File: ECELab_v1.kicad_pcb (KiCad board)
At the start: 2 copper layers, 121 parts, among them J201 USB_C_Receptacle_USB2.0, J202 Conn_01x02_Male, J301 Conn_01x04_Male, J302 Conn_01x03_Male, J501 Conn_01x12_Male, SW301 SW_SPDT, U201 AZ1117IH-3.3TRG1, U301 SN74LVC257AD, U302 FT232HL, U303 93LC56BT-I/OT, U401 MCP23S17_SS, U402 MCP23S17_SS, U403 MCP23S17_SS, U404 MCP23S17_SS, U405 MCP23S17_SS, U406 MCP23S17_SS, U407 MCP23S17_SS, U408 MCP23S17_SS, U501 ICE40-HX8K_Breakout_Board, Y301 12MHz

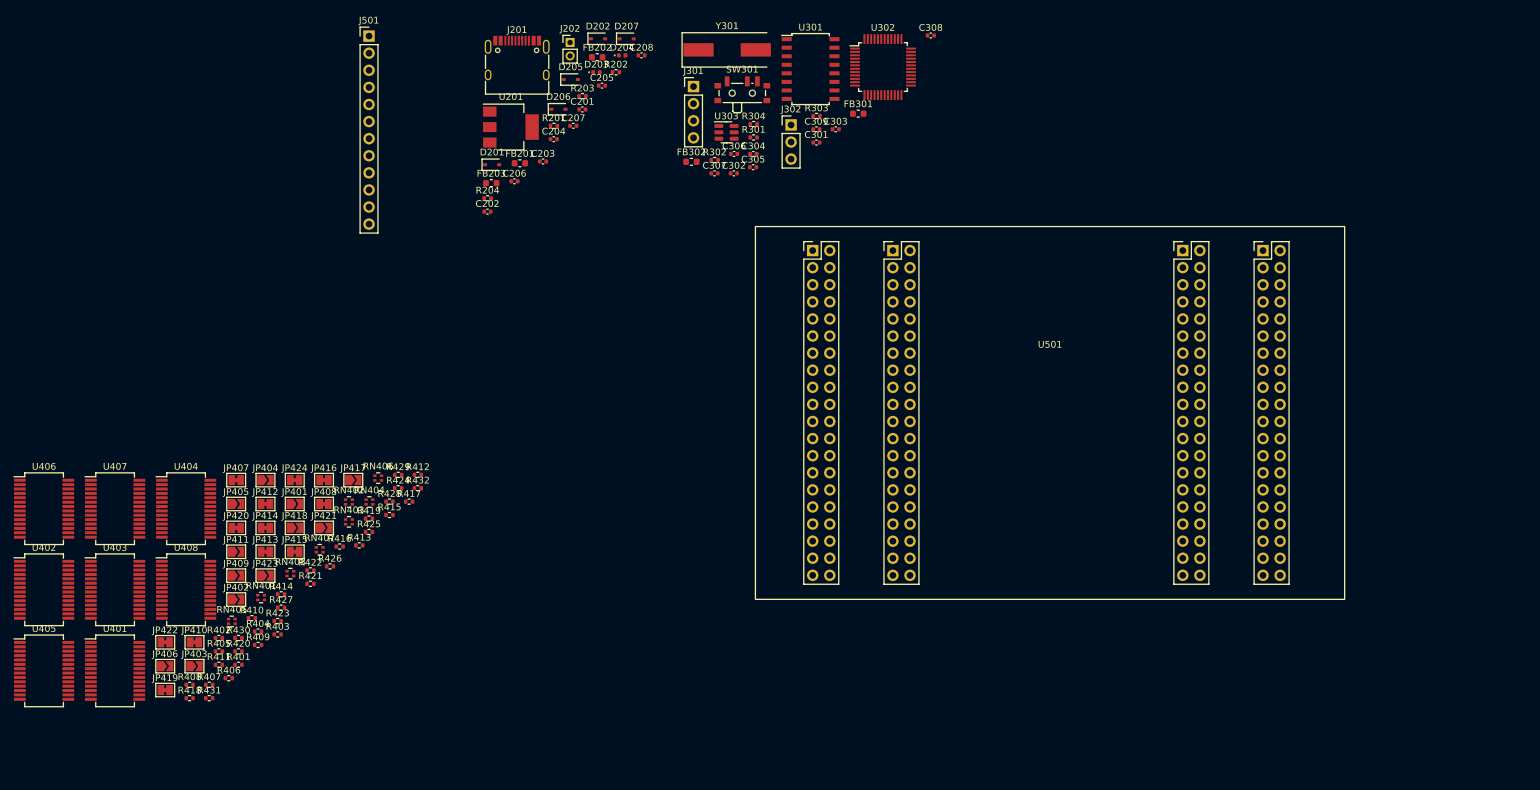
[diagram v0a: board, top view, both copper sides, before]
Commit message: Complete SPI Design
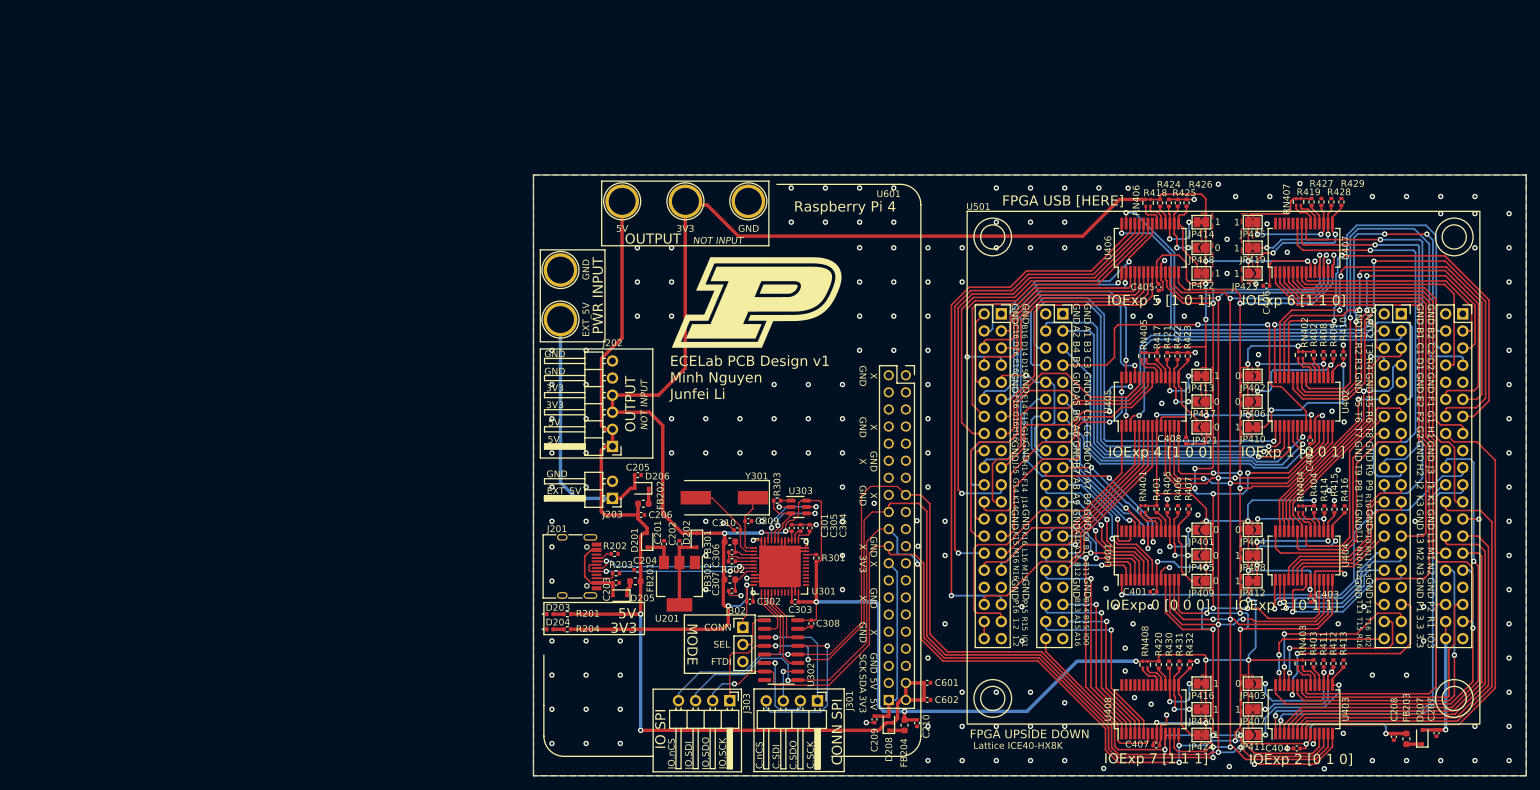
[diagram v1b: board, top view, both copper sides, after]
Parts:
- removed J501: Conn_01x12_Male, Connector_PinHeader_2.54mm:PinHeader_1x12_P2.54mm_Vertical
- removed the R303 at (146.0, 54.1)
- removed SW301: SW_SPDT, Button_Switch_SMD:SW_SPDT_PCM12
- removed the U301 at (145.1, 47.1)
- added C209: 0.1u, Capacitor_SMD:C_0402_1005Metric, F.Cu at (154.6, 143.7)
- added C210: 0.1u, Capacitor_SMD:C_0402_1005Metric, F.Cu at (160.9, 144.3)
- added C308: 0.1u, Capacitor_SMD:C_0402_1005Metric, F.Cu at (145.2, 129.5)
- added C401: 0.1u, Capacitor_SMD:C_0402_1005Metric, F.Cu at (196.1, 124.8)
- added C402: 0.1u, Capacitor_SMD:C_0402_1005Metric, F.Cu at (219.3, 102.3)
- added C403: 0.1u, Capacitor_SMD:C_0402_1005Metric, F.Cu at (219.4, 125.8)
- added C404: 0.1u, Capacitor_SMD:C_0402_1005Metric, F.Cu at (217.4, 148.1)
- added C405: 0.1u, Capacitor_SMD:C_0402_1005Metric, F.Cu at (196.8, 79.5)
- added C406: 0.1u, Capacitor_SMD:C_0402_1005Metric, F.Cu at (212.9, 79.3)
- added C407: 0.1u, Capacitor_SMD:C_0402_1005Metric, F.Cu at (196.5, 147.6)
- added C408: 0.1u, Capacitor_SMD:C_0402_1005Metric, F.Cu at (200.9, 102.3)
- added C601: 0.1u, Capacitor_SMD:C_0402_1005Metric, F.Cu at (162.5, 138.3)
- added C602: 0.1u, Capacitor_SMD:C_0402_1005Metric, F.Cu at (162.5, 140.8)
- added D208: PMEG40, Diode_SMD:D_SOD-323, F.Cu at (156.8, 144.3)
- added FB204: 120R, Inductor_SMD:L_0603_1608Metric, F.Cu at (159.1, 144.6)
- added G***: LOGO, ECELab_Footprints:purduelogo, F.Cu at (137.2, 81.8)
- added G***: LOGO, ECELab_Footprints:purduelogo, B.Cu at (137.9, 81.8)
- added J202: Conn_01x06_Male, Connector_PinHeader_2.54mm:PinHeader_1x06_P2.54mm_Horizontal, F.Cu at (115.7, 103.2)
- added J303: Conn_01x04_Male, Connector_PinHeader_2.54mm:PinHeader_1x04_P2.54mm_Horizontal, F.Cu at (133.1, 141.0)
- added TP201: TestPoint, TestPoint:TestPoint_Plated_Hole_D4.0mm, F.Cu at (117.1, 66.8)
- added TP202: TestPoint, TestPoint:TestPoint_Plated_Hole_D4.0mm, F.Cu at (126.5, 66.8)
- added TP203: TestPoint, TestPoint:TestPoint_Plated_Hole_D4.0mm, F.Cu at (135.9, 66.8)
- added TP204: TestPoint, TestPoint:TestPoint_Plated_Hole_D4.0mm, F.Cu at (108.0, 84.3)
- added TP205: TestPoint, TestPoint:TestPoint_Plated_Hole_D4.0mm, F.Cu at (108.0, 77.0)
- added U302: SN74LVC157ADR, Package_SO:SOIC-16_3.9x9.9mm_P1.27mm, F.Cu at (140.7, 133.5)
- added U601: RASPBERRY_PI_4B_4GB, ECELab_Footprints:MODULE_RASPBERRY_PI_4B_4GB, F.Cu at (134.3, 107.5)
- J203: renamed from J202; footprint Connector_PinHeader_2.00mm:PinHeader_1x02_P2.00mm_Vertical -> Connector_PinHeader_2.54mm:PinHeader_1x02_P2.54mm_Horizontal
- J301: footprint Connector_PinHeader_2.54mm:PinHeader_1x04_P2.54mm_Vertical -> Connector_PinHeader_2.54mm:PinHeader_1x04_P2.54mm_Horizontal
- R201: value 250 -> 220
- U301: renamed from U302; value FT232HL -> FT232HQ-REEL; footprint Package_QFP:LQFP-48_7x7mm_P0.5mm -> Package_DFN_QFN:QFN-48-1EP_8x8mm_P0.5mm_EP6.2x6.2mm
- U401, U402, U403, U404, U405, U406, U407, U408: value MCP23S17_SS -> MCP23017_SS
- moved U402 189.3 mm to (218.4, 96.5), turned to 90 degrees
- moved U407 180.9 mm to (218.4, 73.7), turned to 90 degrees
- moved U403 177.6 mm to (218.4, 142.2), turned to 90 degrees
- moved R408 175.5 mm to (221.3, 89.6), turned to 90 degrees
- moved JP419 174.5 mm to (210.8, 73.7)
- moved U405 169.2 mm to (195.6, 96.5), turned to 90 degrees
- moved U406 168.9 mm to (195.6, 73.7), turned to 90 degrees
- moved R402 168.1 mm to (219.9, 89.6), turned to -90 degrees
- moved R410 166.9 mm to (224.3, 89.6), turned to 90 degrees
- moved JP406 166.3 mm to (210.8, 96.5)
- moved U404 166.3 mm to (218.4, 119.4), turned to 90 degrees
- moved R427 165.9 mm to (221.0, 66.8), turned to 90 degrees
- moved R409 165.5 mm to (222.8, 89.6), turned to 90 degrees
- moved R411 164.2 mm to (221.4, 135.4), turned to 90 degrees
- moved JP422 163.5 mm to (203.2, 77.5), turned to 180 degrees
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- renumbered C308 to C309, C309 to C310, R304 to R303
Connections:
- net IO44 renamed IO.SS2_4
- J301 pad 2: CONN.SDI -> CONN.SDO
- J301 pad 3: CONN.SDO -> CONN.SDI
- J302 pad 2: MUX.SEL -> SEL
- U301 pad 14: FTDI.SDI -> FTDI.SDO
- U301 pad 15: FTDI.SDO -> FTDI.SDI
- U401 pad 1: IO0 -> IO.HWCLK
- U401 pad 13: IO.SDI -> IO.SDO
- U401 pad 14: IO.SDO -> IO.SDI
- U401 pad 2: IO1 -> IO.PB20
- U401 pad 21: IO8 -> IO.PB13
- U401 pad 22: IO9 -> IO.PB12
- U401 pad 23: IO10 -> IO.PB11
- U401 pad 24: IO11 -> IO.PB10
- U401 pad 25: IO12 -> IO.PB9
- U401 pad 26: IO13 -> IO.PB8
- U401 pad 27: IO14 -> unconnected-(U401-Pad27)
- U401 pad 28: IO15 -> unconnected-(U401-Pad28)
- U401 pad 3: IO2 -> IO.PB19
- U401 pad 4: IO3 -> IO.PB18
- U401 pad 5: IO4 -> IO.PB17
- U401 pad 6: IO5 -> IO.PB16
- U401 pad 7: IO6 -> IO.PB15
- U401 pad 8: IO7 -> IO.PB14
- U402 pad 1: IO16 -> IO.PB7
- U402 pad 13: IO.SDI -> IO.SDO
- U402 pad 14: IO.SDO -> IO.SDI
- U402 pad 2: IO17 -> IO.PB6
- U402 pad 21: IO24 -> IO.SS0_0
- U402 pad 22: IO25 -> IO.SS0_1
- U402 pad 23: IO26 -> IO.SS0_2
- U402 pad 24: IO27 -> IO.SS0_3
- U402 pad 25: IO28 -> IO.SS0_4
- U402 pad 26: IO29 -> IO.SS0_5
- U402 pad 27: IO30 -> IO.SS0_6
- U402 pad 28: IO31 -> IO.SS0_7
- U402 pad 3: IO18 -> IO.PB5
- U402 pad 4: IO19 -> IO.PB4
- U402 pad 5: IO20 -> IO.PB3
- U402 pad 6: IO21 -> IO.PB2
- U402 pad 7: IO22 -> IO.PB1
- U402 pad 8: IO23 -> IO.PB0
- U403 pad 1: IO32 -> IO.SS1_0
- U403 pad 13: IO.SDI -> IO.SDO
- U403 pad 14: IO.SDO -> IO.SDI
- U403 pad 2: IO33 -> IO.SS1_1
- U403 pad 21: IO40 -> IO.SS2_0
- U403 pad 22: IO41 -> IO.SS2_1
- U403 pad 23: IO42 -> IO.SS2_2
- U403 pad 24: IO43 -> IO.SS2_3
- U403 pad 26: IO45 -> IO.SS2_5
- U403 pad 27: IO46 -> IO.SS2_6
- U403 pad 28: IO47 -> IO.SS2_7
- U403 pad 3: IO34 -> IO.SS1_2
- U403 pad 4: IO35 -> IO.SS1_3
- U403 pad 5: IO36 -> IO.SS1_4
- U403 pad 6: IO37 -> IO.SS1_5
- U403 pad 7: IO38 -> IO.SS1_6
- U403 pad 8: IO39 -> IO.SS1_7
- U404 pad 1: IO48 -> IO.SS3_0
- U404 pad 13: IO.SDI -> IO.SDO
- U404 pad 14: IO.SDO -> IO.SDI
- U404 pad 2: IO49 -> IO.SS3_1
- U404 pad 21: IO56 -> /GPIO Expansion/IO.SS4_0
- U404 pad 22: IO57 -> /GPIO Expansion/IO.SS4_1
- U404 pad 23: IO58 -> /GPIO Expansion/IO.SS4_2
- U404 pad 24: IO59 -> /GPIO Expansion/IO.SS4_3
- U404 pad 25: IO60 -> /GPIO Expansion/IO.SS4_4
- U404 pad 26: IO61 -> /GPIO Expansion/IO.SS4_5
- U404 pad 27: IO62 -> /GPIO Expansion/IO.SS4_6
- U404 pad 28: IO63 -> /GPIO Expansion/IO.SS4_7
- U404 pad 3: IO50 -> IO.SS3_2
- U404 pad 4: IO51 -> IO.SS3_3
- U404 pad 5: IO52 -> IO.SS3_4
- U404 pad 6: IO53 -> IO.SS3_5
- U404 pad 7: IO54 -> IO.SS3_6
- U404 pad 8: IO55 -> IO.SS3_7
- U405 pad 1: IO64 -> /GPIO Expansion/IO.SS5_0
- U405 pad 13: IO.SDI -> IO.SDO
- U405 pad 14: IO.SDO -> IO.SDI
- U405 pad 2: IO65 -> /GPIO Expansion/IO.SS5_1
- U405 pad 21: IO72 -> /GPIO Expansion/IO.SS6_0
- U405 pad 22: IO73 -> /GPIO Expansion/IO.SS6_1
- U405 pad 23: IO74 -> /GPIO Expansion/IO.SS6_2
- U405 pad 24: IO75 -> /GPIO Expansion/IO.SS6_3
- U405 pad 25: IO76 -> /GPIO Expansion/IO.SS6_4
- U405 pad 26: IO77 -> /GPIO Expansion/IO.SS6_5
- U405 pad 27: IO78 -> /GPIO Expansion/IO.SS6_6
- U405 pad 28: IO79 -> /GPIO Expansion/IO.SS6_7
- U405 pad 3: IO66 -> /GPIO Expansion/IO.SS5_2
- U405 pad 4: IO67 -> /GPIO Expansion/IO.SS5_3
- U405 pad 5: IO68 -> /GPIO Expansion/IO.SS5_4
- U405 pad 6: IO69 -> /GPIO Expansion/IO.SS5_5
- U405 pad 7: IO70 -> /GPIO Expansion/IO.SS5_6
- U405 pad 8: IO71 -> /GPIO Expansion/IO.SS5_7
- U406 pad 1: IO80 -> /GPIO Expansion/IO.SS7_0
- U406 pad 13: IO.SDI -> IO.SDO
- U406 pad 14: IO.SDO -> IO.SDI
- U406 pad 2: IO81 -> /GPIO Expansion/IO.SS7_1
- U406 pad 21: IO88 -> IO.LEFT7
- U406 pad 22: IO89 -> IO.LEFT6
- U406 pad 23: IO90 -> IO.LEFT5
- U406 pad 24: IO91 -> IO.LEFT4
- U406 pad 25: IO92 -> IO.LEFT3
- U406 pad 26: IO93 -> IO.LEFT2
- U406 pad 27: IO94 -> IO.LEFT1
- U406 pad 28: IO95 -> IO.LEFT0
- U406 pad 3: IO82 -> /GPIO Expansion/IO.SS7_2
- U406 pad 4: IO83 -> /GPIO Expansion/IO.SS7_3
- U406 pad 5: IO84 -> /GPIO Expansion/IO.SS7_4
- U406 pad 6: IO85 -> /GPIO Expansion/IO.SS7_5
- U406 pad 7: IO86 -> /GPIO Expansion/IO.SS7_6
- U406 pad 8: IO87 -> /GPIO Expansion/IO.SS7_7
- U407 pad 1: IO96 -> IO.RIGHT7
- U407 pad 13: IO.SDI -> IO.SDO
- U407 pad 14: IO.SDO -> IO.SDI
- U407 pad 2: IO97 -> IO.RIGHT6
- U407 pad 21: IO104 -> IO.RED
- U407 pad 22: IO105 -> IO.GREEN
- U407 pad 23: IO106 -> IO.BLUE
- U407 pad 24: IO107 -> unconnected-(U407-Pad24)
- U407 pad 25: IO108 -> unconnected-(U407-Pad25)
- U407 pad 26: IO109 -> unconnected-(U407-Pad26)
- U407 pad 27: IO110 -> unconnected-(U407-Pad27)
- U407 pad 28: IO111 -> unconnected-(U407-Pad28)
- U407 pad 3: IO98 -> IO.RIGHT5
- U407 pad 4: IO99 -> IO.RIGHT4
- U407 pad 5: IO100 -> IO.RIGHT3
- U407 pad 6: IO101 -> IO.RIGHT2
- U407 pad 7: IO102 -> IO.RIGHT1
- U407 pad 8: IO103 -> IO.RIGHT0
- U408 pad 1: IO112 -> IO.Rx
- U408 pad 13: IO.SDI -> IO.SDO
- U408 pad 14: IO.SDO -> IO.SDI
- U408 pad 2: IO113 -> IO.Tx
- U408 pad 21: IO120 -> unconnected-(U408-Pad21)
- U408 pad 22: IO121 -> unconnected-(U408-Pad22)
- U408 pad 23: IO122 -> unconnected-(U408-Pad23)
- U408 pad 24: IO123 -> unconnected-(U408-Pad24)
- U408 pad 25: IO124 -> unconnected-(U408-Pad25)
- U408 pad 26: IO125 -> unconnected-(U408-Pad26)
- U408 pad 27: IO126 -> unconnected-(U408-Pad27)
- U408 pad 28: IO127 -> unconnected-(U408-Pad28)
- U408 pad 3: IO114 -> IO.DSRn
- U408 pad 4: IO115 -> IO.RTSn
- U408 pad 5: IO116 -> IO.DCDn
- U408 pad 6: IO117 -> IO.CTSn
- U408 pad 7: IO118 -> IO.DTRn
- U408 pad 8: IO119 -> unconnected-(U408-Pad8)
- U501 pad 100: IO81 -> IO.PB13
- U501 pad 101: IO65 -> IO.PB14
- U501 pad 102: IO80 -> IO.PB15
- U501 pad 103: IO66 -> IO.PB16
- U501 pad 104: IO79 -> IO.PB17
- U501 pad 107: IO67 -> IO.PB18
- U501 pad 108: IO78 -> IO.PB19
- U501 pad 109: IO68 -> IO.Rx
- U501 pad 11: IO3 -> IO.SS0_6
- U501 pad 110: IO77 -> IO.PB20
- U501 pad 111: IO69 -> /GPIO Expansion/IO.SS5_7
- U501 pad 112: IO76 -> IO.Tx
- U501 pad 115: IO70 -> IO.DSRn
- U501 pad 116: IO75 -> IO.RTSn
- U501 pad 117: IO71 -> IO.DCDn
- U501 pad 118: IO74 -> IO.CTSn
- U501 pad 119: IO72 -> unconnected-(U501-Pad119)
- U501 pad 12: IO24 -> IO.SS0_5
- U501 pad 120: IO73 -> IO.DTRn
- U501 pad 123: IO88 -> /GPIO Expansion/IO.SS7_3
- U501 pad 124: IO115 -> IO.LEFT7
- U501 pad 125: IO89 -> /GPIO Expansion/IO.SS7_5
- U501 pad 126: IO114 -> /GPIO Expansion/IO.SS7_4
- U501 pad 127: IO90 -> IO.LEFT6
- U501 pad 128: IO113 -> /GPIO Expansion/IO.SS7_6
- U501 pad 13: IO4 -> IO.SS0_4
- U501 pad 131: IO91 -> /GPIO Expansion/IO.SS7_1
- U501 pad 132: IO112 -> /GPIO Expansion/IO.SS7_0
- U501 pad 133: IO92 -> /GPIO Expansion/IO.SS7_7
- U501 pad 134: IO111 -> /GPIO Expansion/IO.SS7_2
- U501 pad 135: IO93 -> /GPIO Expansion/IO.SS6_3
- U501 pad 136: IO110 -> IO.LEFT5
- U501 pad 139: IO94 -> /GPIO Expansion/IO.SS6_5
- U501 pad 14: IO23 -> IO.SS0_3
- U501 pad 140: IO109 -> /GPIO Expansion/IO.SS6_4
- U501 pad 141: IO95 -> IO.LEFT4
- U501 pad 142: IO108 -> /GPIO Expansion/IO.SS6_6
- U501 pad 143: IO96 -> /GPIO Expansion/IO.SS6_1
- U501 pad 144: IO107 -> /GPIO Expansion/IO.SS6_0
- U501 pad 147: IO97 -> /GPIO Expansion/IO.SS6_7
- U501 pad 148: IO106 -> /GPIO Expansion/IO.SS6_2
- U501 pad 149: IO98 -> /GPIO Expansion/IO.SS5_3
- U501 pad 15: IO5 -> IO.RIGHT2
- U501 pad 150: IO105 -> IO.LEFT3
- U501 pad 151: IO99 -> /GPIO Expansion/IO.SS5_5
- U501 pad 152: IO104 -> /GPIO Expansion/IO.SS5_4
- U501 pad 155: IO100 -> IO.LEFT2
- U501 pad 156: IO103 -> /GPIO Expansion/IO.SS5_6
- U501 pad 157: IO101 -> /GPIO Expansion/IO.SS5_0
- U501 pad 159: IO102 -> unconnected-(U501-Pad159)
- U501 pad 16: IO22 -> IO.SS1_7
- U501 pad 19: IO6 -> IO.HWCLK
- U501 pad 20: IO21 -> IO.SS1_2
- U501 pad 21: IO7 -> IO.SS1_1
- U501 pad 22: IO20 -> IO.SS1_0
- U501 pad 23: IO8 -> IO.RIGHT3
- U501 pad 24: IO19 -> IO.SS1_6
- U501 pad 27: IO9 -> IO.SS1_5
- U501 pad 28: IO18 -> IO.SS1_4
- U501 pad 29: IO10 -> IO.SS1_3
- U501 pad 3: IO0 -> IO.RIGHT0
- U501 pad 30: IO17 -> IO.RIGHT4
- U501 pad 31: IO11 -> IO.SS2_7
- U501 pad 32: IO16 -> IO.SS2_2
- U501 pad 35: IO12 -> IO.SS2_1
- U501 pad 36: IO15 -> IO.SS2_0
- U501 pad 37: IO13 -> IO.RIGHT5
- U501 pad 39: IO14 -> unconnected-(U501-Pad39)
- U501 pad 4: IO27 -> IO.SS0_7
- U501 pad 43: IO28 -> /GPIO Expansion/IO.SS5_2
- U501 pad 44: IO57 -> /GPIO Expansion/IO.SS5_1
- U501 pad 45: IO29 -> /GPIO Expansion/IO.SS4_3
- U501 pad 46: IO56 -> IO.LEFT1
- U501 pad 47: IO30 -> /GPIO Expansion/IO.SS4_5
- U501 pad 48: IO55 -> /GPIO Expansion/IO.SS4_4
- U501 pad 5: IO1 -> IO.SS0_2
- U501 pad 51: IO31 -> IO.LEFT0
- U501 pad 52: IO54 -> /GPIO Expansion/IO.SS4_6
- U501 pad 53: IO32 -> /GPIO Expansion/IO.SS4_1
- U501 pad 54: IO53 -> /GPIO Expansion/IO.SS4_0
- U501 pad 55: IO33 -> /GPIO Expansion/IO.SS4_7
- U501 pad 56: IO52 -> /GPIO Expansion/IO.SS4_2
- U501 pad 59: IO34 -> IO.BLUE
- U501 pad 6: IO26 -> IO.SS0_1
- U501 pad 60: IO51 -> IO.GREEN
- U501 pad 61: IO35 -> IO.SS3_3
- U501 pad 62: IO50 -> IO.RED
- U501 pad 63: IO36 -> IO.SS3_5
- U501 pad 64: IO49 -> IO.SS3_4
- U501 pad 67: IO37 -> IO.RIGHT7
- U501 pad 68: IO48 -> IO.SS3_6
- U501 pad 69: IO38 -> IO.SS3_1
- U501 pad 7: IO2 -> IO.SS0_0
- U501 pad 70: IO47 -> IO.SS3_0
- U501 pad 71: IO39 -> IO.SS3_7
- U501 pad 72: IO46 -> IO.SS3_2
- U501 pad 75: IO40 -> IO.SS2_3
- U501 pad 76: IO45 -> IO.RIGHT6
- U501 pad 77: IO41 -> IO.SS2_5
- U501 pad 79: IO42 -> unconnected-(U501-Pad79)
- U501 pad 8: IO25 -> IO.RIGHT1
- U501 pad 80: IO43 -> IO.SS2_6
- U501 pad 83: IO58 -> IO.PB4
- U501 pad 84: IO87 -> IO.PB5
- U501 pad 85: IO59 -> IO.PB1
- U501 pad 86: IO86 -> IO.PB6
- U501 pad 87: IO60 -> IO.PB0
- U501 pad 88: IO85 -> IO.PB7
- U501 pad 91: IO61 -> IO.PB2
- U501 pad 92: IO84 -> IO.PB8
- U501 pad 93: IO62 -> IO.PB3
- U501 pad 94: IO83 -> IO.PB9
- U501 pad 95: IO63 -> IO.PB10
- U501 pad 96: IO82 -> IO.PB11
- U501 pad 99: IO64 -> IO.PB12
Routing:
- net +3V3: track 0.00 -> 678.8 mm, vias 0 -> 33
- net IO.~{CS}: track 0.00 -> 335.2 mm, vias 0 -> 13
- net IO.SDI: track 0.00 -> 323.5 mm, vias 0 -> 14
- net IO.SCK: track 0.00 -> 323.1 mm, vias 0 -> 10
- net IO.SDO: track 0.00 -> 315.4 mm, vias 0 -> 10
- net GND: track 0.00 -> 182.1 mm, vias 0 -> 211
- net +5V: track 0.00 -> 153.6 mm, vias 0 -> 2
- net IO.LEFT2: track 0.00 -> 84.1 mm, vias 0 -> 1
- net IO.RIGHT5: track 0.00 -> 77.8 mm
- net IO.RIGHT6: track 0.00 -> 77.7 mm
- net IO.SS1_7: track 0.00 -> 74.4 mm
- net IO.SS0_3: track 0.00 -> 73.8 mm, vias 0 -> 2
- net IO.LEFT3: track 0.00 -> 73.4 mm, vias 0 -> 1
- net IO.SS1_2: track 0.00 -> 71.1 mm, vias 0 -> 1
- net IO.LEFT0: track 0.00 -> 70.1 mm, vias 0 -> 1
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- added copper zone on F.Cu, net +3V3
- added copper zone on B.Cu, net GND
- added copper zone on F.Cu, net GND
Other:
- board outline added: 147.5 x 89.3 mm
- board text added: "0"
- board text added: "1"
- board text added: "3V3"
- board text added: "5V"
- board text added: "5V 3V3"
- board text added: "5V SDA"
- board text added: "A1 A2"
- board text added: "A7 A8"
- board text added: "B10 A11"
- board text added: "B11 B12"
- board text added: "B14 B13"
- board text added: "B15 A15"
- board text added: "B16 C16"
- board text added: "B2 B1"
- board text added: "B3 B4"
- board text added: "B9 A9"
- board text added: "C.SCK"
- board text added: "C.SDI"
- board text added: "C.SDO"
- board text added: "C.nCS"
- board text added: "C2 C1"
- board text added: "C3 B5"
- board text added: "C4 A5"
- board text added: "C5 B6"
- board text added: "C6 A6"
- board text added: "C7 B7"
- board text added: "C9 A10"
- board text added: "CONN"
- board text added: "CONN SPI"
- board text added: "D14 D16"
- board text added: "D15 E16"
- board text added: "D2 D1"
- board text added: "E14 F16"
- board text added: "ECELab PCB Design v1 Minh Nguyen Junfei Li"
- board text added: "EXT_5V"
- board text added: "F1 E2"
- board text added: "F14 G14"
- board text added: "F15 G16"
- board text added: "FPGA USB [HERE]"
- board text added: "FTDI"
- board text added: "G1 F2"
- board text added: "G15 H16"
- board text added: "GND"
- board text added: "GND GND"
- board text added: "GND SCK"
- board text added: "GND X"
- board text added: "H1 G2"
- board text added: "H14 J15"
- board text added: "IO SPI"
- board text added: "IO.SCK"
- board text added: "IO.SDI"
- board text added: "IO.SDO"
- board text added: "IO.nCS"
- board text added: "IO0 A16"
- board text added: "IO1 1.2"
- board text added: "IO2 R16"
- board text added: "IO3 3.3"
- board text added: "IOExp 0 [0 0 0]"
- board text added: "IOExp 1 [0 0 1]"
- board text added: "IOExp 2 [0 1 0]"
- board text added: "IOExp 3 [0 1 1]"
- board text added: "IOExp 4 [1 0 0]"
- board text added: "IOExp 5 [1 0 1]"
- board text added: "IOExp 6 [1 1 0]"
- board text added: "IOExp 7 [1 1 1]"
- board text added: "J1 J2"
- board text added: "J14 K14"
- board text added: "J3 H2"
- board text added: "K1 K3"
- board text added: "K16 K15"
- board text added: "L1 L3"
- board text added: "L16 M16"
- board text added: "M1 M2"
- board text added: "M11 N10"
- board text added: "M15 N16"
- board text added: "MODE"
- board text added: "N2 N3"
- board text added: "NOT INPUT"
- board text added: "OUTPUT"
- board text added: "P10 T11"
- board text added: "P13 N12"
- board text added: "P15 P16"
- board text added: "P2 P1"
- board text added: "P9 P8"
- board text added: "PWR INPUT"
- board text added: "R1 3.3"
- board text added: "R10 T10"
- board text added: "R15 1.2"
- board text added: "R4 R3"
- board text added: "R5 T5"
- board text added: "R6 T6"
- board text added: "R9 T9"
- board text added: "Raspberry Pi 4"
- board text added: "SEL"
- board text added: "T14 T13"
- board text added: "T16 T15"
- board text added: "T2 T1"
- board text added: "T3 R2"
- board text added: "T8 T7"
- board text added: "X 3V3"
- board text added: "X GND"

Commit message: Update 1
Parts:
- removed the J202 at (115.7, 103.2)
- removed J303: Conn_01x04_Male, Connector_PinHeader_2.54mm:PinHeader_1x04_P2.54mm_Horizontal
- removed JP401, JP402, JP403, JP404, JP405, JP406, JP409, JP411, JP417, JP418, JP421, JP423: Jumper_2_Open, Jumper:SolderJumper-2_P1.3mm_Open_TrianglePad1.0x1.5mm
- removed JP407, JP408, JP410, JP412, JP413, JP414, JP415, JP416, JP419, JP420, JP422, JP424: Jumper_2_Bridged, Jumper:SolderJumper-2_P1.3mm_Bridged_Pad1.0x1.5mm
- removed the R405 at (198.1, 112.5)
- removed the R406 at (199.7, 112.5)
- removed the R407 at (201.3, 112.5)
- removed the R408 at (221.3, 89.6)
- removed R409, R410, R411, R412, R413, R414, R415, R416, R421, R422, R423, R424, R425, R426, R427, R428, R429, R430, R431, R432: 10k, Resistor_SMD:R_0402_1005Metric
- removed TP201, TP202, TP203, TP204, TP205: TestPoint, TestPoint:TestPoint_Plated_Hole_D4.0mm
- added R301: 10k, Resistor_SMD:R_0402_1005Metric, F.Cu at (227.4, 229.8)
- added R302: 10k, Resistor_SMD:R_0402_1005Metric, F.Cu at (230.3, 229.8)
- U501: moved to B.Cu
- moved J202 162.4 mm to (65.6, 265.4)
- moved G*** 148.3 mm to (67.9, 212.9)
- moved G*** 148.0 mm to (69.4, 213.0)
- moved C205 133.5 mm to (199.0, 214.6)
- moved C303 133.5 mm to (222.4, 233.5)
- moved C305 133.5 mm to (223.2, 222.5)
- moved D201 133.5 mm to (200.4, 224.3)
- moved D202 133.5 mm to (207.8, 224.3)
- moved J201 133.5 mm to (188.8, 228.2)
- moved R304 133.5 mm to (213.0, 227.4)
- moved U303 133.5 mm to (222.9, 219.3)
- moved C201 133.5 mm to (202.9, 224.8)
- moved C202 133.5 mm to (205.2, 224.8)
- moved C203 133.5 mm to (195.8, 230.6)
- moved C204 133.5 mm to (199.0, 228.7)
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- renumbered J203 to J202, R301 to R303, R302 to R304, R303 to R305, R417 to R405, R418 to R406, R419 to R407, R420 to R408
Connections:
- net /GPIO Expansion/IO.SS4_0 renamed IO.SS4_0
- net /GPIO Expansion/IO.SS4_1 renamed IO.SS4_1
- net /GPIO Expansion/IO.SS4_2 renamed IO.SS4_2
- net /GPIO Expansion/IO.SS4_3 renamed IO.SS4_3
- net /GPIO Expansion/IO.SS4_4 renamed IO.SS4_4
- net /GPIO Expansion/IO.SS4_5 renamed IO.SS4_5
- net /GPIO Expansion/IO.SS4_6 renamed IO.SS4_6
- net /GPIO Expansion/IO.SS4_7 renamed IO.SS4_7
- net /GPIO Expansion/IO.SS5_0 renamed IO.SS5_0
- net /GPIO Expansion/IO.SS5_1 renamed IO.SS5_1
- net /GPIO Expansion/IO.SS5_2 renamed IO.SS5_2
- net /GPIO Expansion/IO.SS5_3 renamed IO.SS5_3
- net /GPIO Expansion/IO.SS5_4 renamed IO.SS5_4
- net /GPIO Expansion/IO.SS5_5 renamed IO.SS5_5
- net /GPIO Expansion/IO.SS5_6 renamed IO.SS5_6
- net /GPIO Expansion/IO.SS5_7 renamed IO.SS5_7
- net /GPIO Expansion/IO.SS6_0 renamed IO.SS6_0
- net /GPIO Expansion/IO.SS6_1 renamed IO.SS6_1
- net /GPIO Expansion/IO.SS6_2 renamed IO.SS6_2
- net /GPIO Expansion/IO.SS6_3 renamed IO.SS6_3
- net /GPIO Expansion/IO.SS6_4 renamed IO.SS6_4
- net /GPIO Expansion/IO.SS6_5 renamed IO.SS6_5
- net /GPIO Expansion/IO.SS6_6 renamed IO.SS6_6
- net /GPIO Expansion/IO.SS6_7 renamed IO.SS6_7
- net /GPIO Expansion/IO.SS7_0 renamed IO.SS7_0
- net /GPIO Expansion/IO.SS7_1 renamed IO.SS7_1
- net /GPIO Expansion/IO.SS7_2 renamed IO.SS7_2
- net /GPIO Expansion/IO.SS7_3 renamed IO.SS7_3
- net /GPIO Expansion/IO.SS7_4 renamed IO.SS7_4
- net /GPIO Expansion/IO.SS7_5 renamed IO.SS7_5
- net /GPIO Expansion/IO.SS7_6 renamed IO.SS7_6
- net /GPIO Expansion/IO.SS7_7 renamed IO.SS7_7
- U301 pad 14: FTDI.SDO -> FTDI.SDA
- U301 pad 15: FTDI.SDI -> unconnected-(U301-Pad15)
- U301 pad 16: FTDI.~{CS} -> unconnected-(U301-Pad16)
- U401 pad 11: IO.~{CS} -> unconnected-(U401-Pad11)
- U401 pad 13: IO.SDO -> IO.SDA
- U401 pad 14: IO.SDI -> unconnected-(U401-Pad14)
- U401 pad 15: Net-(JP409-Pad2) -> GND
- U401 pad 16: Net-(JP405-Pad2) -> GND
- U401 pad 17: Net-(JP401-Pad2) -> GND
- U402 pad 11: IO.~{CS} -> unconnected-(U402-Pad11)
- U402 pad 13: IO.SDO -> IO.SDA
- U402 pad 14: IO.SDI -> unconnected-(U402-Pad14)
- U402 pad 15: Net-(JP410-Pad2) -> +3V3
- U402 pad 16: Net-(JP406-Pad2) -> GND
- U402 pad 17: Net-(JP402-Pad2) -> GND
- U403 pad 11: IO.~{CS} -> unconnected-(U403-Pad11)
- U403 pad 13: IO.SDO -> IO.SDA
- U403 pad 14: IO.SDI -> unconnected-(U403-Pad14)
- U403 pad 15: Net-(JP411-Pad2) -> GND
- U403 pad 16: Net-(JP407-Pad2) -> +3V3
- U403 pad 17: Net-(JP403-Pad2) -> GND
- U404 pad 11: IO.~{CS} -> unconnected-(U404-Pad11)
- U404 pad 13: IO.SDO -> IO.SDA
- U404 pad 14: IO.SDI -> unconnected-(U404-Pad14)
- U404 pad 15: Net-(JP412-Pad2) -> +3V3
- U404 pad 16: Net-(JP408-Pad2) -> +3V3
- U404 pad 17: Net-(JP404-Pad2) -> GND
- U405 pad 11: IO.~{CS} -> unconnected-(U405-Pad11)
- U405 pad 13: IO.SDO -> IO.SDA
- U405 pad 14: IO.SDI -> unconnected-(U405-Pad14)
- U405 pad 15: Net-(JP421-Pad2) -> GND
- U405 pad 16: Net-(JP417-Pad2) -> GND
- U405 pad 17: Net-(JP413-Pad2) -> +3V3
- U406 pad 11: IO.~{CS} -> unconnected-(U406-Pad11)
- U406 pad 13: IO.SDO -> IO.SDA
- U406 pad 14: IO.SDI -> unconnected-(U406-Pad14)
- U406 pad 15: Net-(JP422-Pad2) -> +3V3
- U406 pad 16: Net-(JP418-Pad2) -> GND
- U406 pad 17: Net-(JP414-Pad2) -> +3V3
- U407 pad 11: IO.~{CS} -> unconnected-(U407-Pad11)
- U407 pad 13: IO.SDO -> IO.SDA
- U407 pad 14: IO.SDI -> unconnected-(U407-Pad14)
- U407 pad 15: Net-(JP423-Pad2) -> GND
- U407 pad 16: Net-(JP419-Pad2) -> +3V3
- U407 pad 17: Net-(JP415-Pad2) -> +3V3
- U408 pad 11: IO.~{CS} -> unconnected-(U408-Pad11)
- U408 pad 13: IO.SDO -> IO.SDA
- U408 pad 14: IO.SDI -> unconnected-(U408-Pad14)
- U408 pad 15: Net-(JP424-Pad2) -> +3V3
- U408 pad 16: Net-(JP420-Pad2) -> +3V3
- U408 pad 17: Net-(JP416-Pad2) -> +3V3
- U501 pad 119: unconnected-(U501-Pad119) -> IO.IO0
- U501 pad 159: unconnected-(U501-Pad159) -> IO.IO1
- U501 pad 39: unconnected-(U501-Pad39) -> IO.IO3
- U501 pad 79: unconnected-(U501-Pad79) -> IO.IO2
- U601 pad 19: IO.SDO -> unconnected-(U601-Pad19)
- U601 pad 21: IO.SDI -> unconnected-(U601-Pad21)
- U601 pad 23: IO.SCK -> unconnected-(U601-Pad23)
- U601 pad 26: IO.~{CS} -> unconnected-(U601-Pad26)
- U601 pad 29: unconnected-(U601-Pad29) -> IO.IO0
- U601 pad 3: unconnected-(U601-Pad3) -> IO.SDA
- U601 pad 31: unconnected-(U601-Pad31) -> IO.IO1
- U601 pad 32: unconnected-(U601-Pad32) -> IO.IO2
- U601 pad 33: unconnected-(U601-Pad33) -> IO.IO3
- U601 pad 5: unconnected-(U601-Pad5) -> IO.SCK
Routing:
- net +3V3: track 678.8 -> 228.3 mm, vias 33 -> 15
- net IO.~{CS}: track 335.2 -> 51.5 mm, vias 13 -> 1
- net IO.SCK: track 323.1 -> 46.7 mm, vias 10 -> 2
- net IO.SDI: track 323.5 -> 48.8 mm, vias 14 -> 1
- net IO.SDO: track 315.4 -> 43.6 mm, vias 10 -> 1
- net GND: track 182.1 -> 92.7 mm, vias 211 -> 18
- net IO.LEFT2: track 84.1 -> 0.00 mm, vias 1 -> 0
- net IO.RIGHT5: track 77.8 -> 0.00 mm
- net IO.RIGHT6: track 77.7 -> 0.00 mm
- net IO.SS1_7: track 74.4 -> 0.00 mm
- net IO.SS0_3: track 73.8 -> 0.00 mm, vias 2 -> 0
- net IO.LEFT3: track 73.4 -> 0.00 mm, vias 1 -> 0
- net IO.SS1_2: track 71.1 -> 0.00 mm, vias 1 -> 0
- net IO.LEFT0: track 70.1 -> 0.00 mm, vias 1 -> 0
- net IO.SS0_4: track 69.8 -> 0.00 mm, vias 2 -> 0
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- added copper zone on In1.Cu, net GND
- added copper zone on In2.Cu, net GND
- removed copper zone on F.Cu, net +3V3
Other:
- board size 147.5 x 89.3 mm -> 82.4 x 76.2 mm
- copper layers 2 -> 4
- board text removed: "0"
- board text removed: "1"
- board text removed: "A1 A2"
- board text removed: "A7 A8"
- board text removed: "B10 A11"
- board text removed: "B11 B12"
- board text removed: "B14 B13"
- board text removed: "B15 A15"
- board text removed: "B16 C16"
- board text removed: "B2 B1"
- board text removed: "B3 B4"
- board text removed: "B9 A9"
- board text removed: "C2 C1"
- board text removed: "C3 B5"
- board text removed: "C4 A5"
- board text removed: "C5 B6"
- board text removed: "C6 A6"
- board text removed: "C7 B7"
- board text removed: "C9 A10"
- board text removed: "D14 D16"
- board text removed: "D15 E16"
- board text removed: "D2 D1"
- board text removed: "E14 F16"
- board text removed: "F1 E2"
- board text removed: "F14 G14"
- board text removed: "F15 G16"
- board text removed: "FPGA USB [HERE]"
- board text removed: "G1 F2"
- board text removed: "G15 H16"
- board text removed: "GND GND"
- board text removed: "H1 G2"
- board text removed: "H14 J15"
- board text removed: "IO0 A16"
- board text removed: "IO1 1.2"
- board text removed: "IO2 R16"
- board text removed: "IO3 3.3"
- board text removed: "J1 J2"
- board text removed: "J14 K14"
- board text removed: "J3 H2"
- board text removed: "K1 K3"
- board text removed: "K16 K15"
- board text removed: "L1 L3"
- board text removed: "L16 M16"
- board text removed: "M1 M2"
- board text removed: "M11 N10"
- board text removed: "M15 N16"
- board text removed: "N2 N3"
- board text removed: "P10 T11"
- board text removed: "P13 N12"
- board text removed: "P15 P16"
- board text removed: "P2 P1"
- board text removed: "P9 P8"
- board text removed: "R1 3.3"
- board text removed: "R10 T10"
- board text removed: "R15 1.2"
- board text removed: "R4 R3"
- board text removed: "R5 T5"
- board text removed: "R6 T6"
- board text removed: "R9 T9"
- board text removed: "T14 T13"
- board text removed: "T16 T15"
- board text removed: "T2 T1"
- board text removed: "T3 R2"
- board text removed: "T8 T7"
